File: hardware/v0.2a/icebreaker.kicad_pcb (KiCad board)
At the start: 4 copper layers, 73 x 37 mm, 115 parts, among them J1 Jumper, J10 Jumper, J11 Jumper, J12 Jumper, J13 Jumper, J14 Jumper, J15 Jumper, J16 Jumper, J17 Jumper, J18 Jumper, J19 Jumper, J2 Jumper, J20 Flash, J21 PMOD_1A, J22 PMOD_1B, J23 PMOD_2H, J24 PMOD_2P, J25 RGB Led, J26 5V AUX, J27 5V AUX, J3 Jumper, J4 Jumper, J5 Jumper, J6 Jumper, J7 Jumper, J8 Jumper, J9 Jumper, P1 pkl_USB_OTG, SW1 TACT, SW2 TACT, SW3 TACT, SW4 TACT, U1 93C46B-SOT-23-6, U2 3.3V, U3 1V2, U4 FT2232H, U5 W25Q, U6 ICE5LP4K-SG48, X1 12MHz

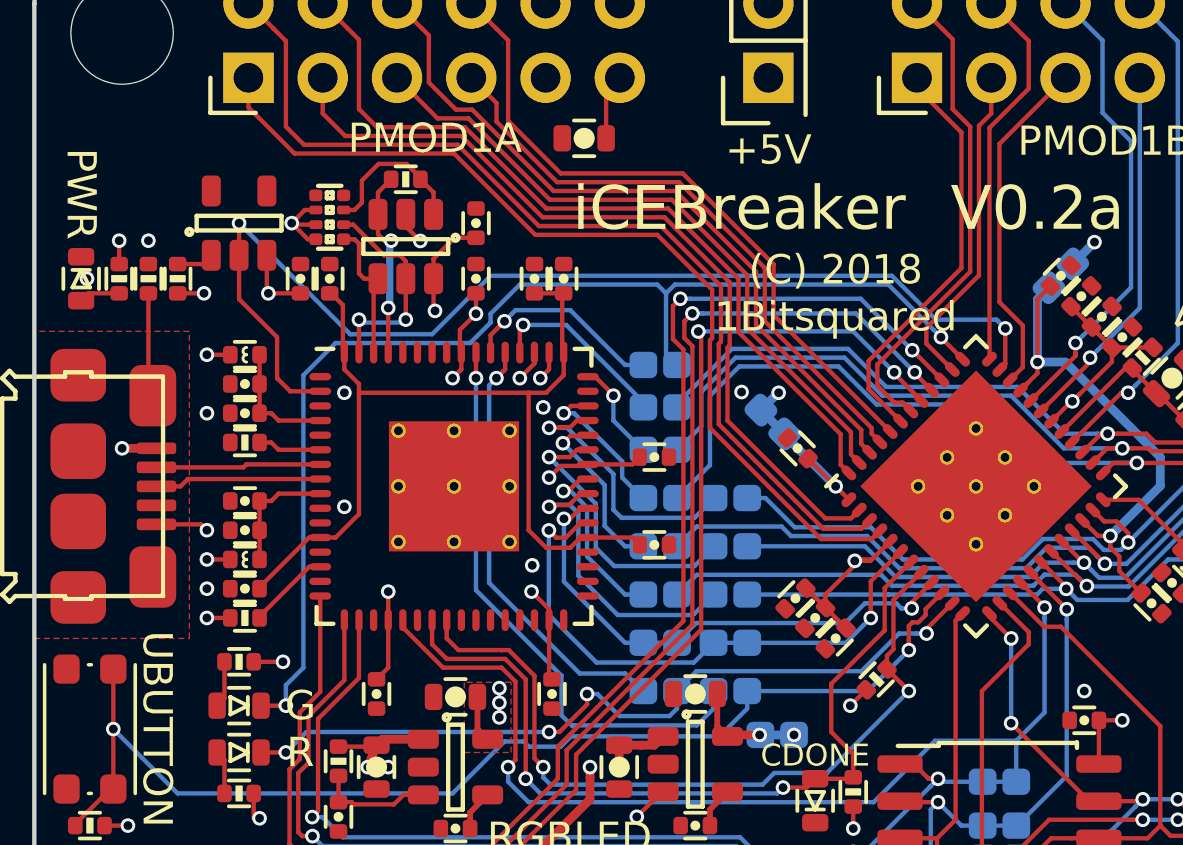
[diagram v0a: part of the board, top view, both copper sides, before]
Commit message: Fixed #6 Oscillator pinout and schematic symbol.
Both bitsy and icebreaker.
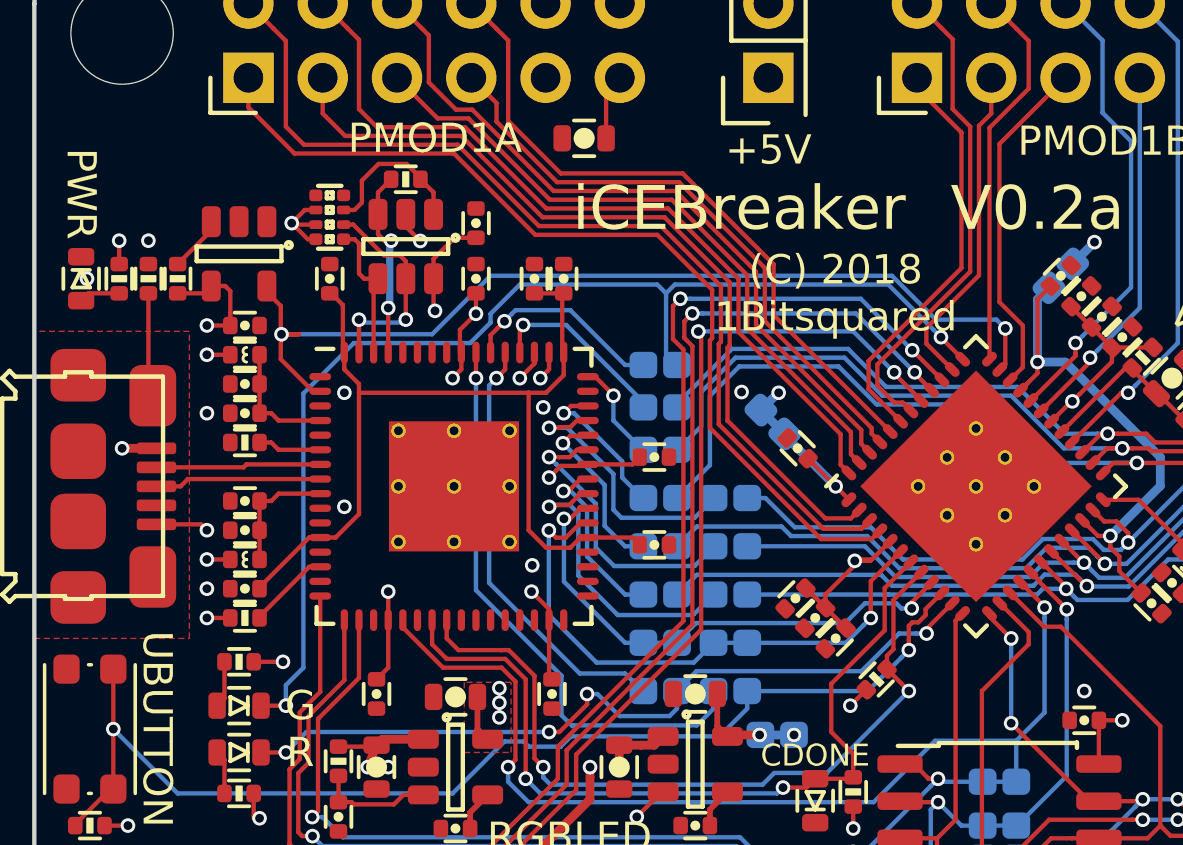
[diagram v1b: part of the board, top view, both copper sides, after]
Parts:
- removed X1: 12MHz, pkl_housings_sot:SOT-23-5
- added U7: 12MHz, pkl_housings_sot:SOT-23-5, F.Cu at (37.0, 39.5)
- moved C4 2.48 mm to (37.2, 42.0), turned to 0 degrees
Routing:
- net /FTDI_CLK: track 38.3 -> 33.5 mm
- net Net-(R7-Pad2): track 1.27 -> 1.93 mm
- net +3V3: track 95.8 -> 96.5 mm, vias 36 -> 35

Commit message: Replaced 0402 4.7u capacitors with 0603 for consistency. Fixes #4
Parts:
- C6, C7, C9: footprint pkl_dipol:C_0402 -> pkl_dipol:C_0603
- moved C12 0.25 mm to (37.2, 43.8)
- moved C13 0.25 mm to (37.2, 49.2)
- moved C14 0.25 mm to (37.2, 51.2)
- moved C4 0.25 mm to (37.2, 41.8)
- moved C7 0.25 mm to (46.9, 40.4)
- moved L1 0.25 mm to (37.2, 50.2)
- moved L2 0.25 mm to (37.2, 42.8)
- moved R8 0.25 mm to (37.2, 46.2)
- moved R9 0.25 mm to (37.2, 52.2)
- moved D1 0.10 mm to (31.6, 40.3)
- moved R1 0.10 mm to (33.9, 40.3)
- moved R5 0.10 mm to (32.9, 40.3)
- moved R7 0.10 mm to (34.9, 40.3)
- moved U7 0.10 mm to (37.0, 39.5)
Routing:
- net /FTDI_CLK: track 33.5 -> 32.7 mm
- net +1V8: track 32.5 -> 33.3 mm
- net Net-(R9-Pad1): track 2.78 -> 3.45 mm

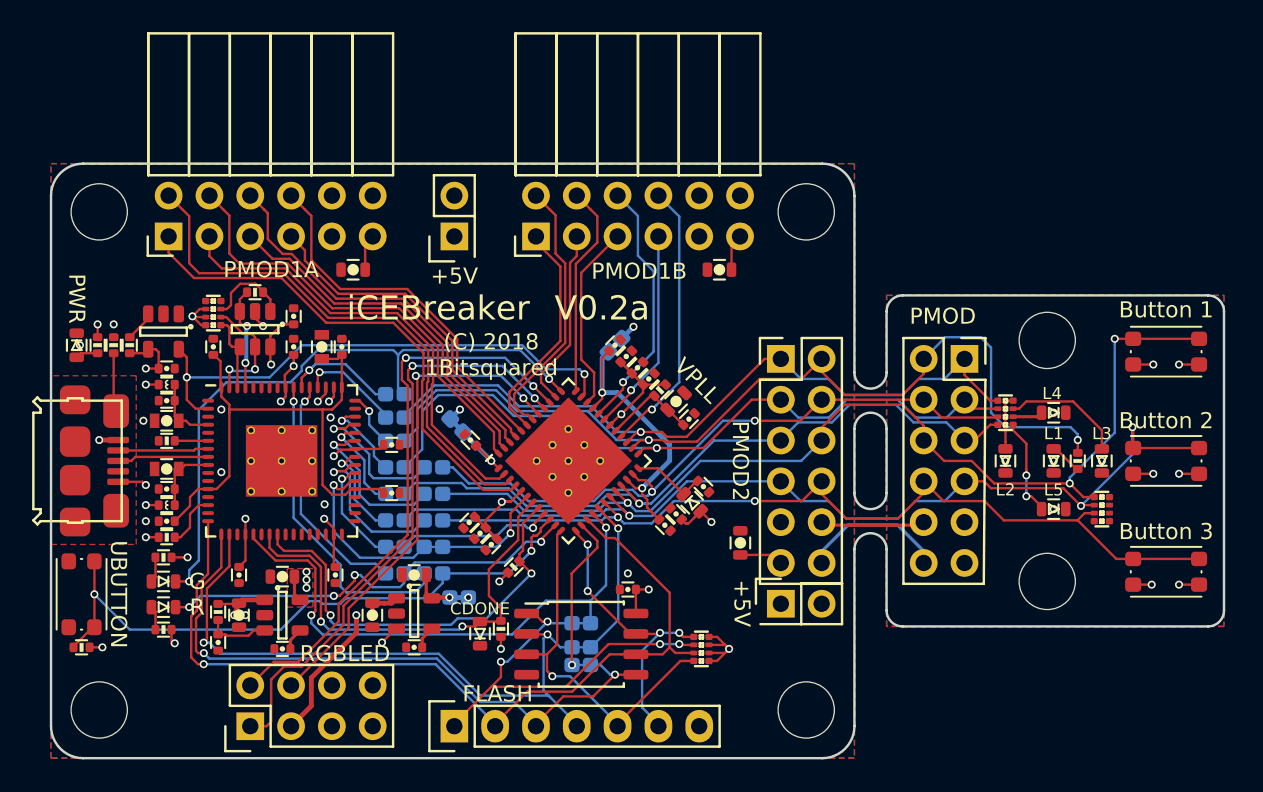
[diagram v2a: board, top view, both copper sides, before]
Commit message: Added inline resistors on all PMOD connectors to allow for higher GPIO speeds.
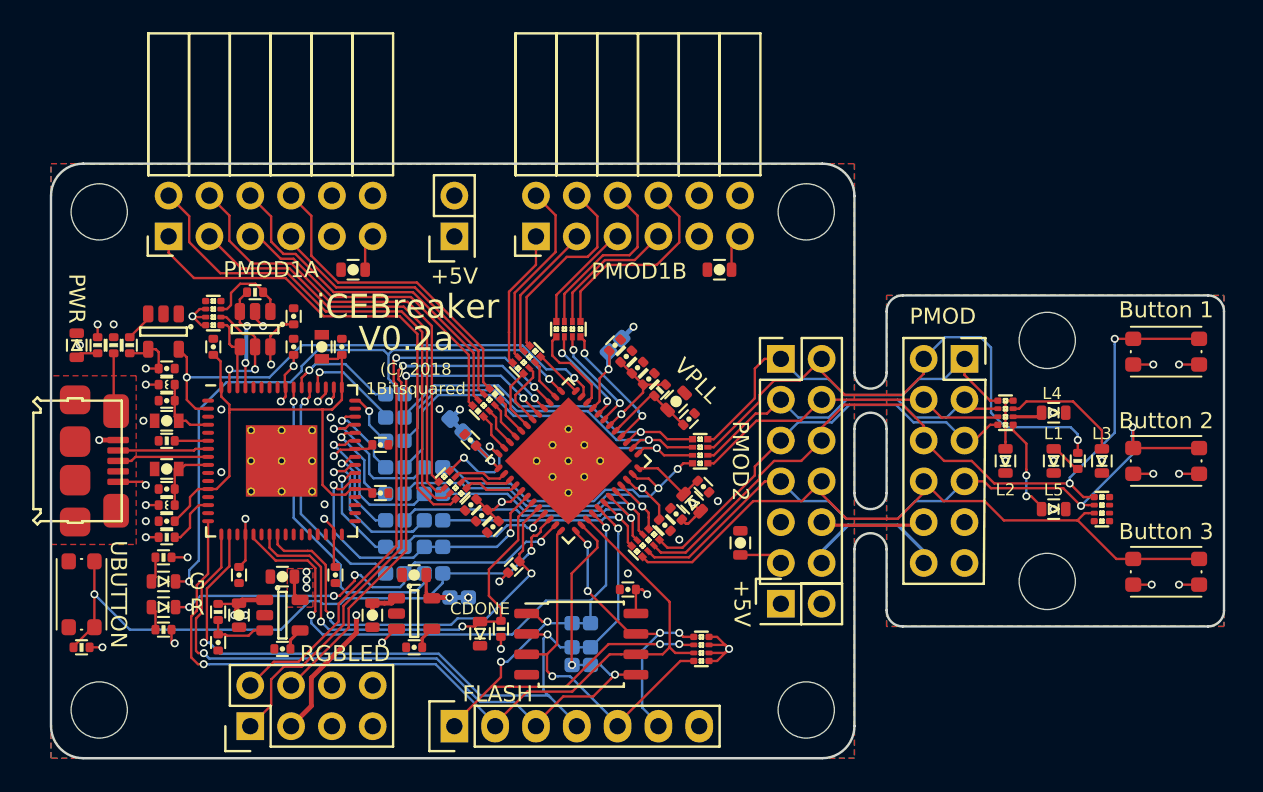
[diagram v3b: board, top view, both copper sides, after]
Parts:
- added R20: 33E, pkl_dipol:R_Array_Convex_4x0402, F.Cu at (55.0, 49.0)
- added R21: 33E, pkl_dipol:R_Array_Convex_4x0402, F.Cu at (59.6, 41.2)
- added R22: 33E, pkl_dipol:R_Array_Convex_4x0402, F.Cu at (67.0, 52.6)
- added R23: 33E, pkl_dipol:R_Array_Convex_4x0402, F.Cu at (57.1, 43.9)
- added R24: 33E, pkl_dipol:R_Array_Convex_4x0402, F.Cu at (62.2, 39.3)
- added R4: 33E, pkl_dipol:R_Array_Convex_4x0402, F.Cu at (70.4, 46.9)
- moved C36 1.10 mm to (57.5, 51.6)
- moved C37 1.10 mm to (56.8, 50.9)
- moved C38 1.10 mm to (56.1, 50.2)
- moved C16 0.70 mm to (50.5, 49.5)
- moved C20 0.70 mm to (50.5, 46.5)
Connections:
- J21 pad 1: /P1A1 -> /P1A1x
- J21 pad 10: /P1A10 -> /P1A10x
- J21 pad 2: /P1A2 -> /P1A2x
- J21 pad 3: /P1A3 -> /P1A3x
- J21 pad 4: /P1A4 -> /P1A4x
- J21 pad 7: /P1A7 -> /P1A7x
- J21 pad 8: /P1A8 -> /P1A8x
- J21 pad 9: /P1A9 -> /P1A9x
- J22 pad 1: /P1B1 -> /P1B1x
- J22 pad 10: /P1B10 -> /P1B10x
- J22 pad 2: /P1B2 -> /P1B2x
- J22 pad 3: /P1B3 -> /P1B3x
- J22 pad 4: /P1B4 -> /P1B4x
- J22 pad 7: /P1B7 -> /P1B7x
- J22 pad 8: /P1B8 -> /P1B8x
- J22 pad 9: /P1B9 -> /P1B9x
- J23 pad 1: /P2_1 -> /P2_1x
- J23 pad 10: /P2_10 -> /P2_10x
- J23 pad 2: /P2_2 -> /P2_2x
- J23 pad 3: /P2_3 -> /P2_3x
- J23 pad 4: /P2_4 -> /P2_4x
- J23 pad 7: /P2_7 -> /P2_7x
- J23 pad 8: /P2_8 -> /P2_8x
- J23 pad 9: /P2_9 -> /P2_9x
- J24 pad 1: /P2_1 -> /P2_1x
- J24 pad 10: /P2_10 -> /P2_10x
- J24 pad 2: /P2_2 -> /P2_2x
- J24 pad 3: /P2_3 -> /P2_3x
- J24 pad 4: /P2_4 -> /P2_4x
- J24 pad 7: /P2_7 -> /P2_7x
- J24 pad 8: /P2_8 -> /P2_8x
- J24 pad 9: /P2_9 -> /P2_9x
- R16 pad 1: /P2_9 -> /P2_9x
- R16 pad 3: /P2_4 -> /P2_4x
- R16 pad 5: /P2_10 -> /P2_10x
- R17 pad 2: /P2_3 -> /P2_3x
- R17 pad 4: /P2_8 -> /P2_8x
- R17 pad 6: /P2_2 -> /P2_2x
- R17 pad 8: /P2_1 -> /P2_1x
- R18 pad 2: /P2_7 -> /P2_7x
- SW2 pad 1: /P2_9 -> /P2_9x
- SW3 pad 1: /P2_4 -> /P2_4x
- SW4 pad 1: /P2_10 -> /P2_10x
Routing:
- net /P2_9x: track 0.00 -> 50.3 mm, vias 0 -> 2
- net /P2_9: track 64.0 -> 15.9 mm, vias 3 -> 1
- net /P2_4x: track 0.00 -> 44.1 mm, vias 0 -> 2
- net /P2_10x: track 0.00 -> 42.9 mm
- net /P2_4: track 60.5 -> 18.4 mm, vias 3 -> 1
- net /P2_10: track 55.7 -> 14.5 mm, vias 2 -> 1
- net /P2_7: track 58.0 -> 22.6 mm, vias 2 -> 1
- net /P2_7x: track 0.00 -> 35.0 mm, vias 0 -> 1
- net /P1A7x: track 0.00 -> 32.0 mm
- net /P1A1x: track 0.00 -> 31.1 mm
- net /P1A7: track 33.4 -> 3.37 mm
- net /P1A1: track 31.7 -> 3.45 mm
- net /P1A8x: track 0.00 -> 28.0 mm
- net /P1A2x: track 0.00 -> 26.8 mm
- net /P2_3x: track 0.00 -> 26.6 mm
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- removed copper zone on In2.Cu, net +1V2
